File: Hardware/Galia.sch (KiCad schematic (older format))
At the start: 136 parts, among them J1 Bat, J2 OLED, J3 Interconnect, J4 Bat, J5 Trackball, J6 OLED, J7 Interconnect_R, SW1 MX, SW10 MX, SW11 MX, SW12 MX, SW13 MX, SW14 MX, SW15 MX, SW16 MX, SW17 MX, SW18 MX, SW19 MX, SW2 MX, SW20 MX, SW21 MX, SW22 MX, SW23 MX, SW24 MX, SW25 MX, SW26 MX, SW27 MX, SW28 MX, SW29 MX, SW3 MX, SW30 MX, SW31 MX, SW32 MX, SW33 MX, SW34 Encoder, SW35 Reset, SW36 MX, SW37 MX, SW38 MX, SW39 MX, SW4 MX, SW40 MX, SW41 MX, SW42 MX, SW43 MX, SW44 MX, SW45 MX, SW46 MX, SW47 MX, SW48 MX, SW49 MX, SW5 MX, SW50 MX, SW51 MX, SW52 MX, SW53 MX, SW54 MX, SW55 MX, SW56 MX, SW57 MX, SW58 MX, SW59 MX, SW6 MX, SW60 MX, SW61 MX, SW62 MX, SW63 MX, SW64 Reset, SW7 MX, SW8 MX, SW9 MX, U1 ProMicro, U2 ProMicro

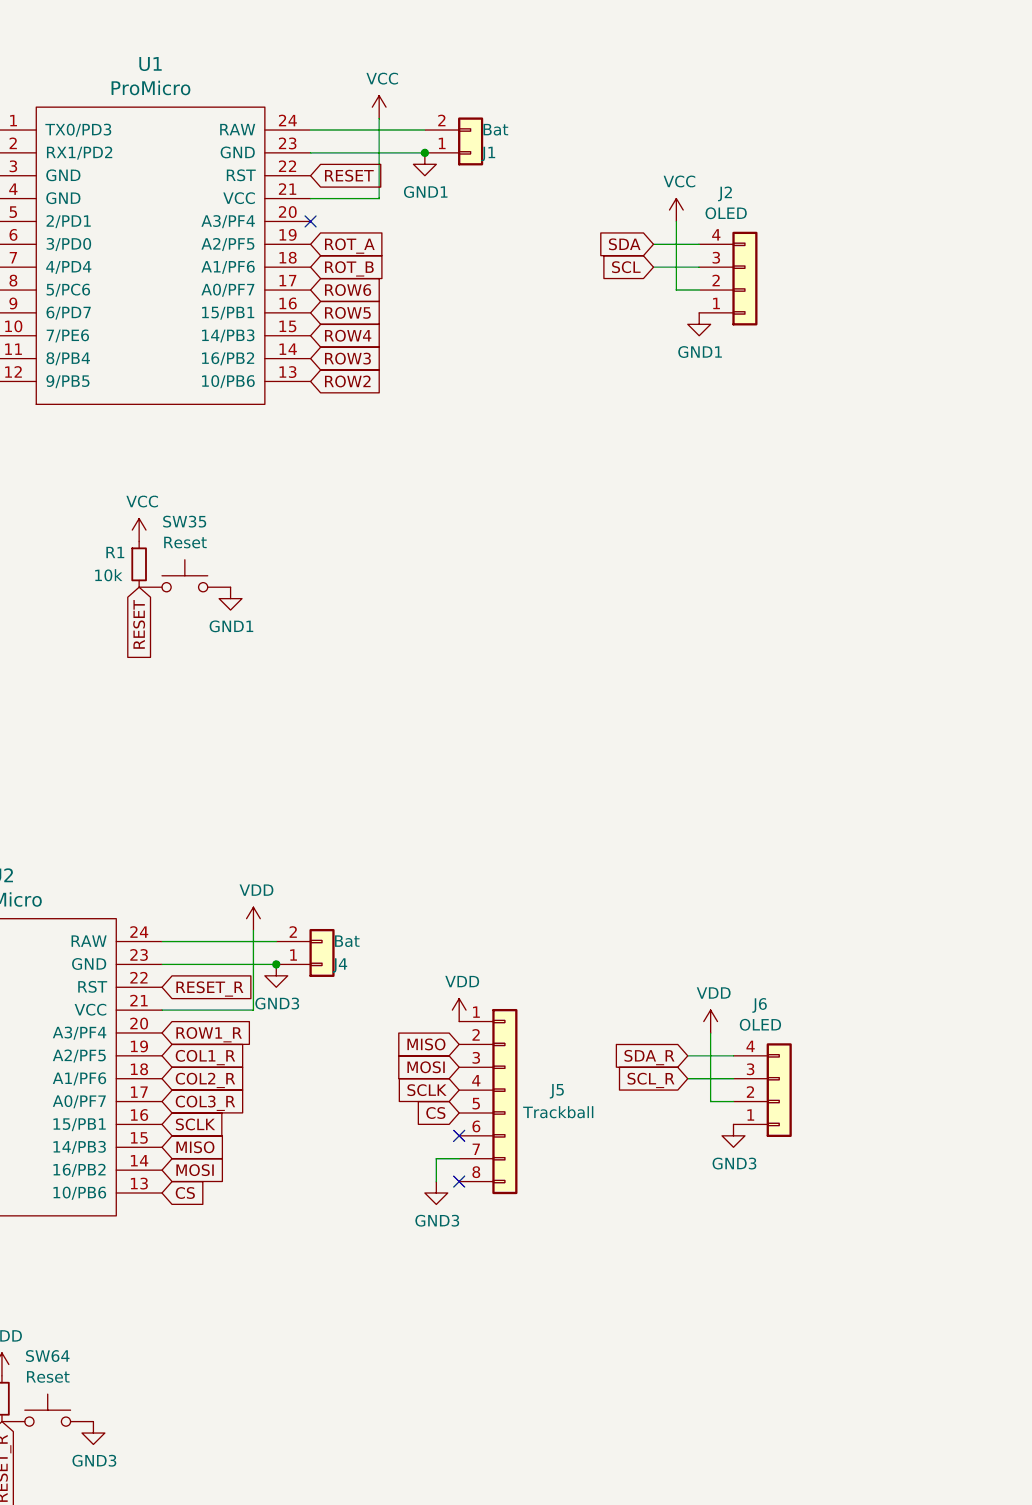
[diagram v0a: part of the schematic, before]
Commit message: Added spot for TP4056 charger
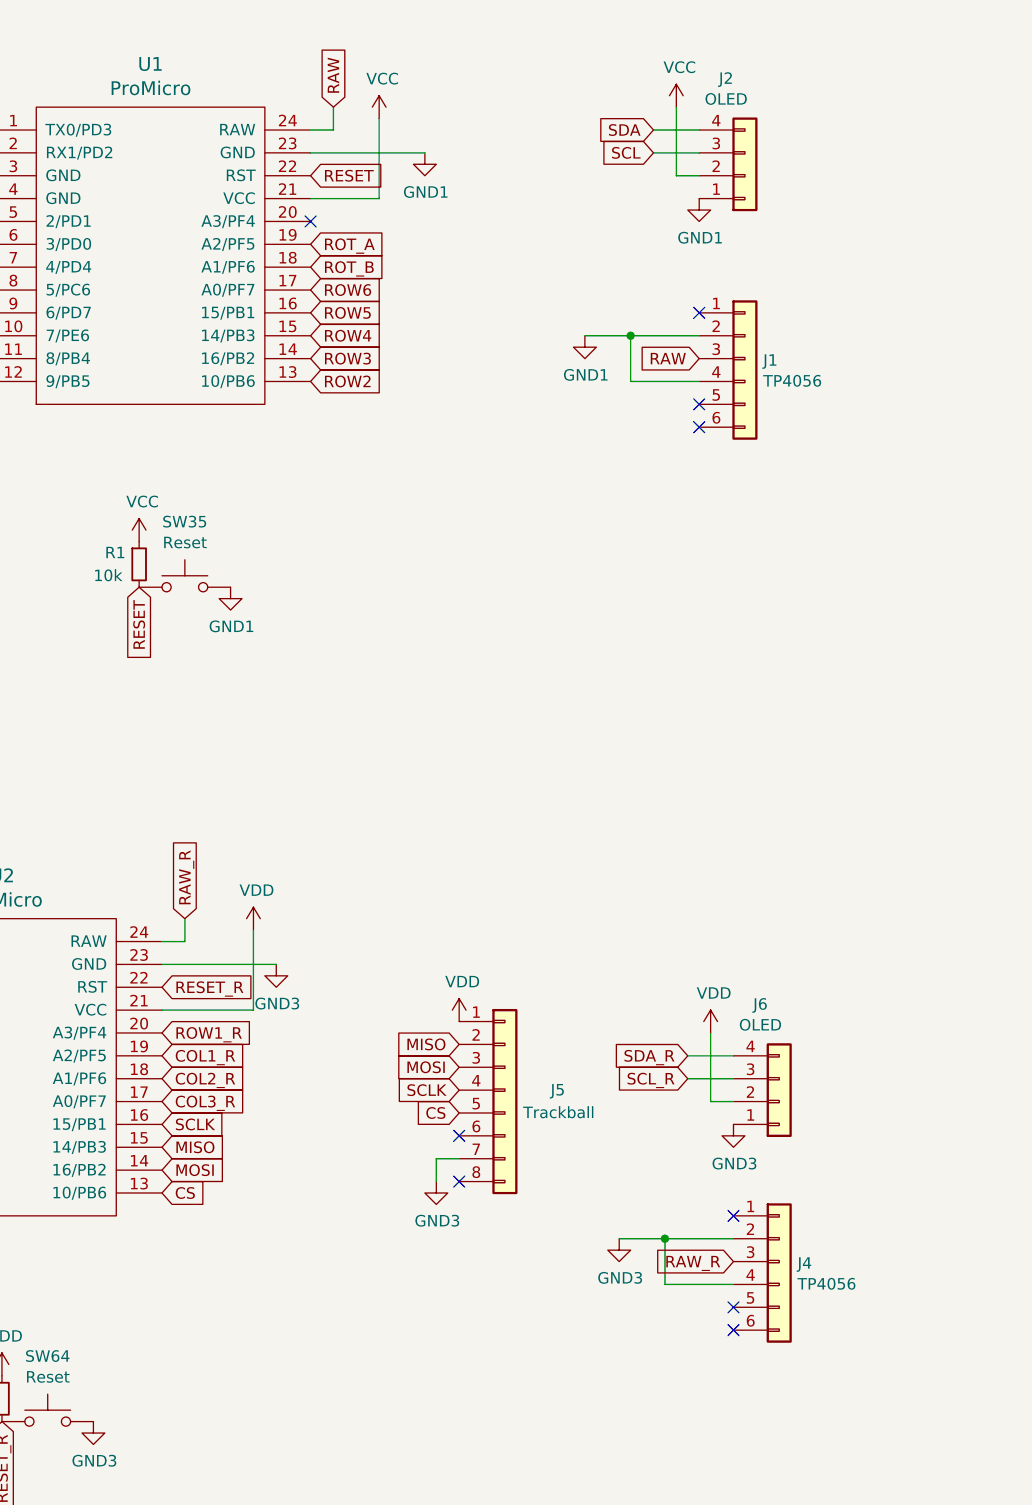
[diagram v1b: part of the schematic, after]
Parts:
- removed J1, J4: Bat, Galia:Battery_Solder_Points, symbol Connector_Generic:Conn_01x02
- added J1, J4: TP4056, Galia:TP4056-18650, symbol Connector_Generic:Conn_01x06
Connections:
- net GND1: now also J1.2 (Pin_2), J1.4 (Pin_4)
- net GND3: now also J4.2 (Pin_2), J4.4 (Pin_4)
- net RAW: now reaches U1.24 (RAW)
- net RAW: now also J1.3 (Pin_3)
- net RAW_R: now reaches U2.24 (RAW)
- net RAW_R: now also J4.3 (Pin_3)
- no-connect marks 7 -> 13
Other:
- moved on the sheet: J2
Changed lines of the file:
@@
 	1    0    0    -1
 $EndComp
-Connection ~ 6300 4700
 $Comp
 L power:GND3 #PWR014
@@
 Wire Wire Line
 	5800 4700 6300 4700
-Wire Wire Line
-	6300 4600 5800 4600
-$Comp
-L Connector_Generic:Conn_01x02 J4
-U 1 1 5F63E50D
-P 6500 4700
-F 0 "J4" H 6550 4700 50  0000 L CNN
-F 1 "Bat" H 6550 4600 50  0000 L CNN
-F 2 "Galia:Battery_Solder_Points" H 6500 4700 50  0001 C CNN
-F 3 "~" H 6500 4700 50  0001 C CNN
-	1    6500 4700
-	1    0    0    1
-$EndComp
 Wire Wire Line
 	6200 4550 6200 4900
@@
 	1    0    0    -1
 $EndComp
-$Comp
-L Connector_Generic:Conn_01x02 J1
-U 1 1 5F53949C
-P 7150 1150
-F 0 "J1" H 7200 1150 50  0000 L CNN
-F 1 "Bat" H 7200 1050 50  0000 L CNN
-F 2 "Galia:Battery_Solder_Points" H 7150 1150 50  0001 C CNN
-F 3 "~" H 7150 1150 50  0001 C CNN
-	1    7150 1150
-	1    0    0    1
-$EndComp
 Wire Wire Line
 	6950 1150 6450 1150
-Connection ~ 6950 1150
-Wire Wire Line
-	6450 1050 6950 1050
 Connection ~ 2550 1350
 Wire Wire Line
@@
 L Connector_Generic:Conn_01x04 J2
 U 1 1 6085DDB0
-P 8350 1750
-F 0 "J2" H 8268 1325 50  0000 C CNN
-F 1 "OLED" H 8268 1416 50  0000 C CNN
-F 2 "Galia:PinHeader_1x04_P2.54mm_Vertical_No_Silk" H 8350 1750 50  0001 C CNN
-F 3 "~" H 8350 1750 50  0001 C CNN
-	1    8350 1750
+P 8350 1250
+F 0 "J2" H 8268 825 50  0000 C CNN
+F 1 "OLED" H 8268 916 50  0000 C CNN
+F 2 "Galia:PinHeader_1x04_P2.54mm_Vertical_No_Silk" H 8350 1250 50  0001 C CNN
+F 3 "~" H 8350 1250 50  0001 C CNN
+	1    8350 1250
 	1    0    0    1
 $EndComp
-Text GLabel 7950 1650 0    50   Input ~ 0
+Text GLabel 7950 1150 0    50   Input ~ 0
 SCL
-Text GLabel 7950 1550 0    50   Input ~ 0
+Text GLabel 7950 1050 0    50   Input ~ 0
 SDA
 $Comp
 L power:GND1 #PWR08
 U 1 1 60869B98
-P 8150 1850
-F 0 "#PWR08" H 8150 1600 50  0001 C CNN
-F 1 "GND1" H 8155 1677 50  0000 C CNN
-F 2 "" H 8150 1850 50  0001 C CNN
-F 3 "" H 8150 1850 50  0001 C CNN
-	1    8150 1850
+P 8150 1350
+F 0 "#PWR08" H 8150 1100 50  0001 C CNN
+F 1 "GND1" H 8155 1177 50  0000 C CNN
+F 2 "" H 8150 1350 50  0001 C CNN
+F 3 "" H 8150 1350 50  0001 C CNN
+	1    8150 1350
 	1    0    0    -1
 $EndComp
@@
 L power:VCC #PWR07
 U 1 1 608AE49E
-P 8050 1450
-F 0 "#PWR07" H 8050 1300 50  0001 C CNN
-F 1 "VCC" H 8065 1623 50  0000 C CNN
-F 2 "" H 8050 1450 50  0001 C CNN
-F 3 "" H 8050 1450 50  0001 C CNN
-	1    8050 1450
-	1    0    0    -1
-$EndComp
-Wire Wire Line
-	8050 1450 8050 1750
-Wire Wire Line
-	8050 1750 8150 1750
-Wire Wire Line
-	7950 1550 8150 1550
-Wire Wire Line
-	8150 1650 7950 1650
+P 8050 950
+F 0 "#PWR07" H 8050 800 50  0001 C CNN
+F 1 "VCC" H 8065 1123 50  0000 C CNN
+F 2 "" H 8050 950 50  0001 C CNN
+F 3 "" H 8050 950 50  0001 C CNN
+	1    8050 950
+	1    0    0    -1
+$EndComp
+Wire Wire Line
+	8050 950  8050 1250
+Wire Wire Line
+	8050 1250 8150 1250
+Wire Wire Line
+	7950 1050 8150 1050
+Wire Wire Line
+	8150 1150 7950 1150
 $Comp
 L Connector_Generic:Conn_01x04 J6
@@
 Wire Wire Line
 	10650 4850 10650 4950
+$Comp
+L Connector_Generic:Conn_01x06 J1
+U 1 1 5F7CF040
+P 8350 2050
+F 0 "J1" H 8430 2042 50  0000 L CNN
+F 1 "TP4056" H 8430 1951 50  0000 L CNN
+F 2 "Galia:TP4056-18650" H 8350 2050 50  0001 C CNN
+F 3 "~" H 8350 2050 50  0001 C CNN
+	1    8350 2050
+	1    0    0    -1
+$EndComp
+$Comp
+L power:GND1 #PWR0105
+U 1 1 5F7DFD8A
+P 7650 1950
+F 0 "#PWR0105" H 7650 1700 50  0001 C CNN
+F 1 "GND1" H 7655 1777 50  0000 C CNN
+F 2 "" H 7650 1950 50  0001 C CNN
+F 3 "" H 7650 1950 50  0001 C CNN
+	1    7650 1950
+	1    0    0    -1
+$EndComp
+Wire Wire Line
+	7850 1950 8150 1950
+Wire Wire Line
+	8150 2150 7850 2150
+Wire Wire Line
+	7850 2150 7850 1950
+Text GLabel 6550 950  1    50   Input ~ 0
+RAW
+Text GLabel 8150 2050 0    50   Input ~ 0
+RAW
+NoConn ~ 8150 1850
+Wire Wire Line
+	7850 1950 7650 1950
+Connection ~ 7850 1950
+$Comp
+L Connector_Generic:Conn_01x06 J4
+U 1 1 5F862446
+P 8500 6000
+F 0 "J4" H 8580 5992 50  0000 L CNN
+F 1 "TP4056" H 8580 5901 50  0000 L CNN
+F 2 "Galia:TP4056-18650" H 8500 6000 50  0001 C CNN
+F 3 "~" H 8500 6000 50  0001 C CNN
+	1    8500 6000
+	1    0    0    -1
+$EndComp
+Wire Wire Line
+	8000 5900 8300 5900
+Wire Wire Line
+	8300 6100 8000 6100
+Wire Wire Line
+	8000 6100 8000 5900
+Text GLabel 8300 6000 0    50   Input ~ 0
+RAW_R
+NoConn ~ 8300 5800
+Wire Wire Line
+	8000 5900 7800 5900
+Connection ~ 8000 5900
+$Comp
+L power:GND3 #PWR0106
+U 1 1 5F926D5F
+P 7800 5900
+F 0 "#PWR0106" H 7800 5650 50  0001 C CNN
+F 1 "GND3" H 7805 5727 50  0000 C CNN
+F 2 "" H 7800 5900 50  0001 C CNN
+F 3 "" H 7800 5900 50  0001 C CNN
+	1    7800 5900
+	1    0    0    -1
+$EndComp
+Text GLabel 5900 4500 1    50   Input ~ 0
+RAW_R
+Wire Wire Line
+	5900 4500 5900 4600
+Wire Wire Line
+	5800 4600 5900 4600
+Wire Wire Line
+	6550 950  6550 1050
+Wire Wire Line
+	6450 1050 6550 1050
+NoConn ~ 8150 2250
+NoConn ~ 8150 2350
+NoConn ~ 8300 6200
+NoConn ~ 8300 6300
 $EndSCHEMATC

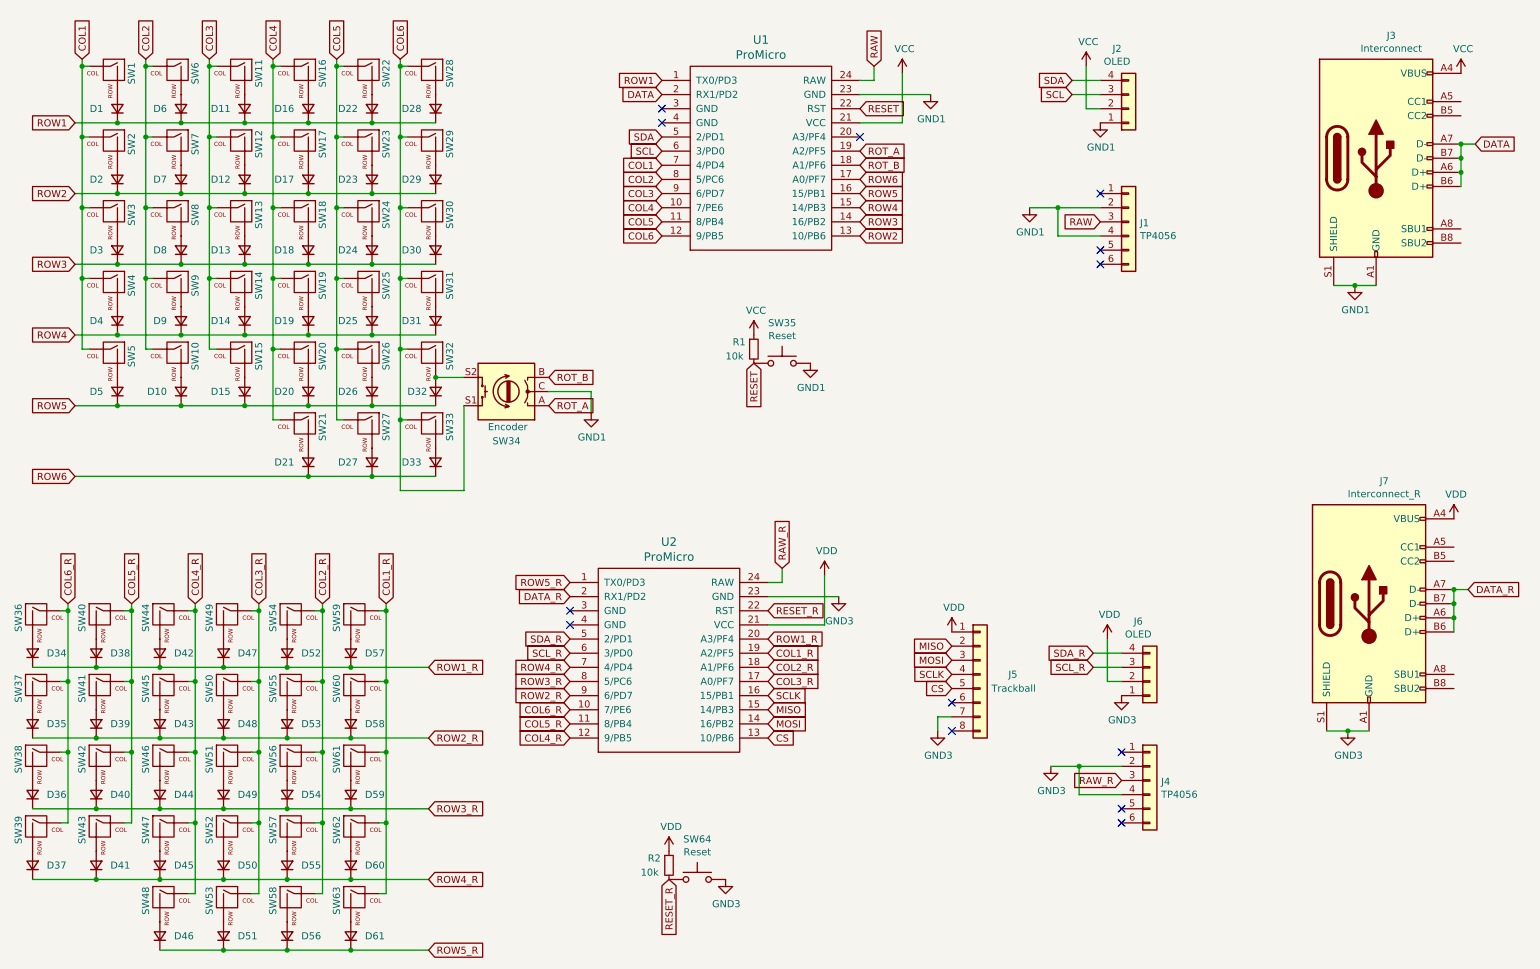
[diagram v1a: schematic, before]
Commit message: Changed reset switch footprint and position, removed pull-up resistor
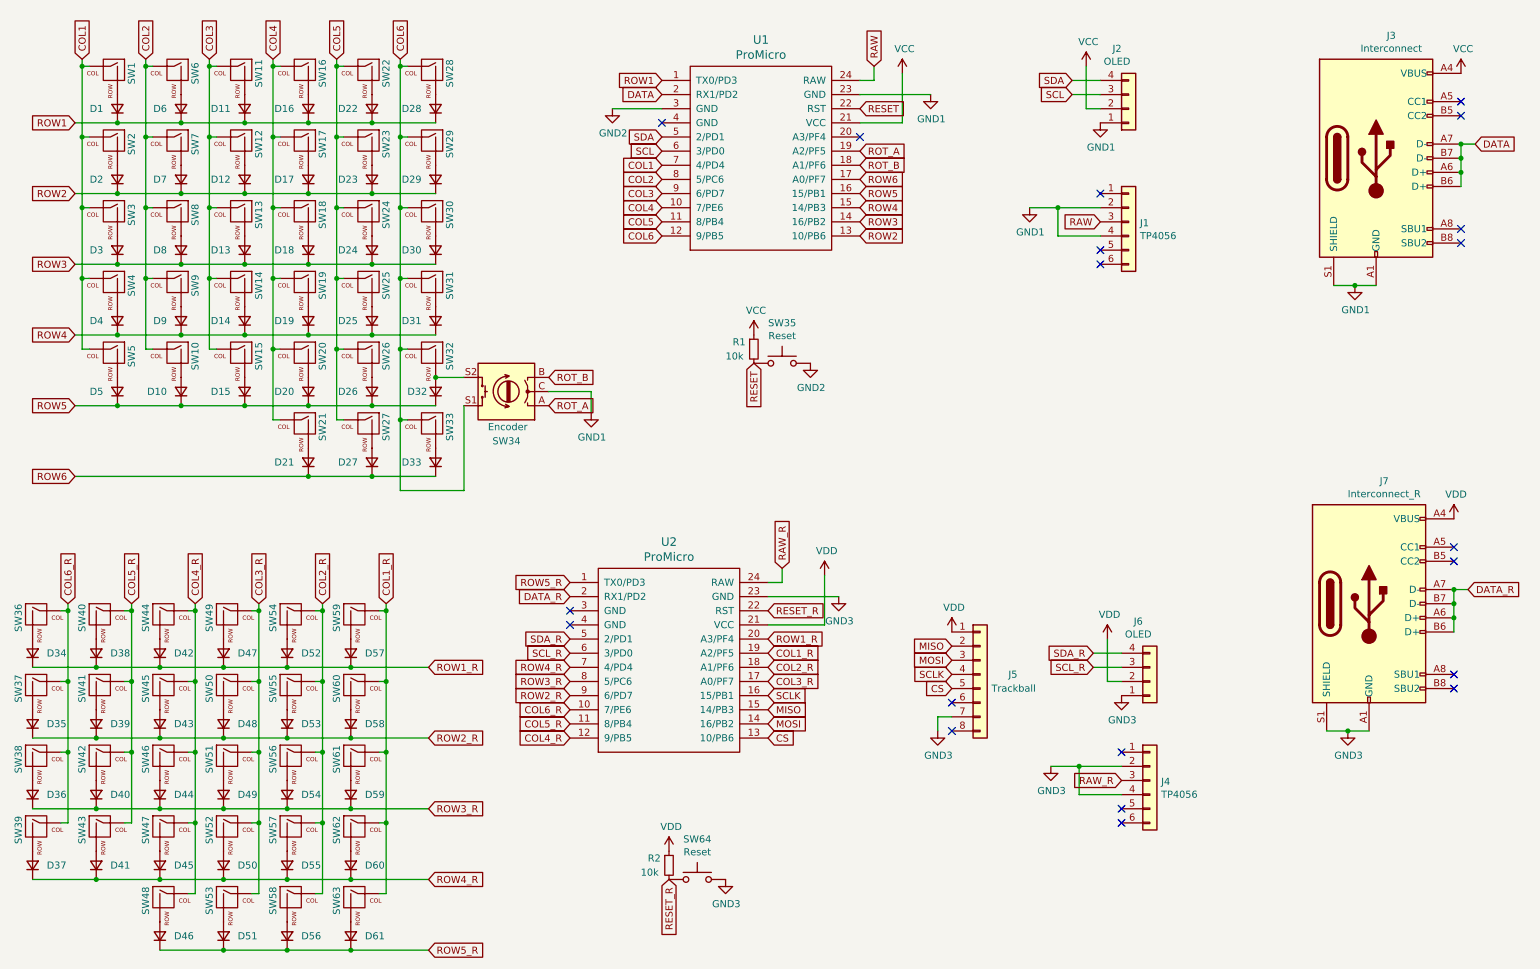
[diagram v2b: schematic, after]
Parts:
- SW35, SW64: footprint Button_Switch_SMD:SW_SPST_TL3342 -> Galia:Switch_Tactile_SPST_Angled_MJTP1117
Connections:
- net GND1: no longer SW35.2
- net GND2: now reaches U1.3 (GND)
- net GND2: now also SW35.2
- no-connect marks 13 -> 20
